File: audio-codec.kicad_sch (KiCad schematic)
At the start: 15 parts, among them J1 AudioJack2_Ground, J2 AudioJack2_Ground, U4 XTAC5112IRGER

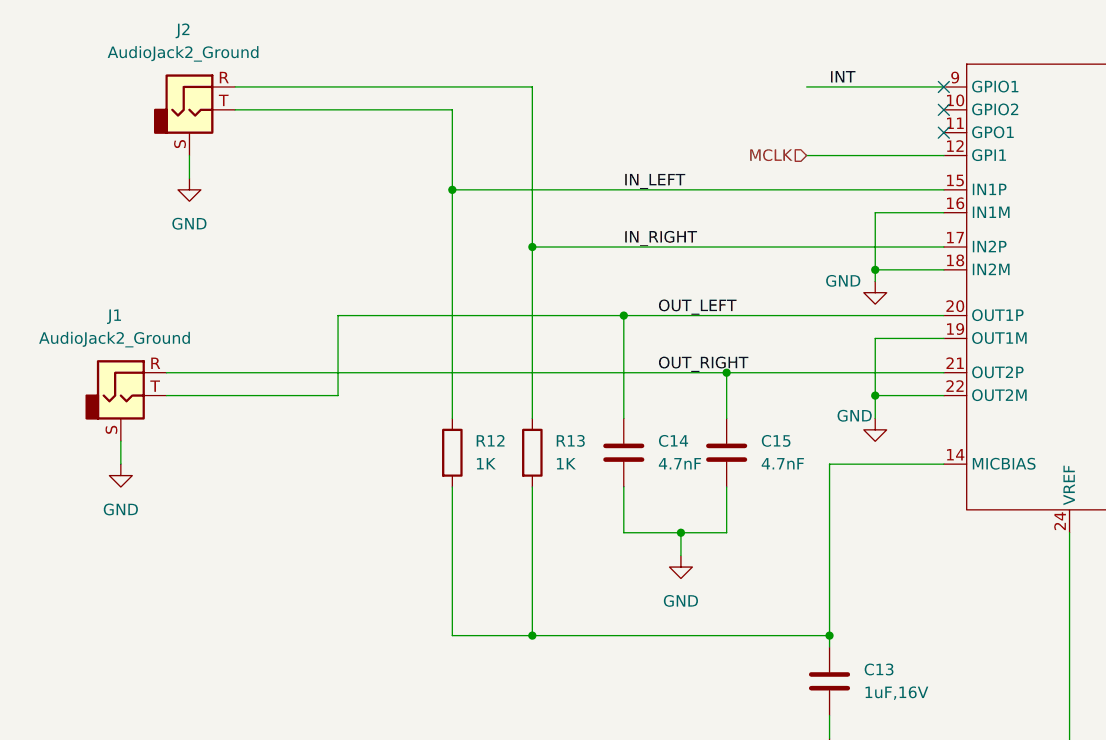
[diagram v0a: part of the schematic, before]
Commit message: Resolved #6: Added connection options for IN_COMMON and OUT_COMMON for audio codec
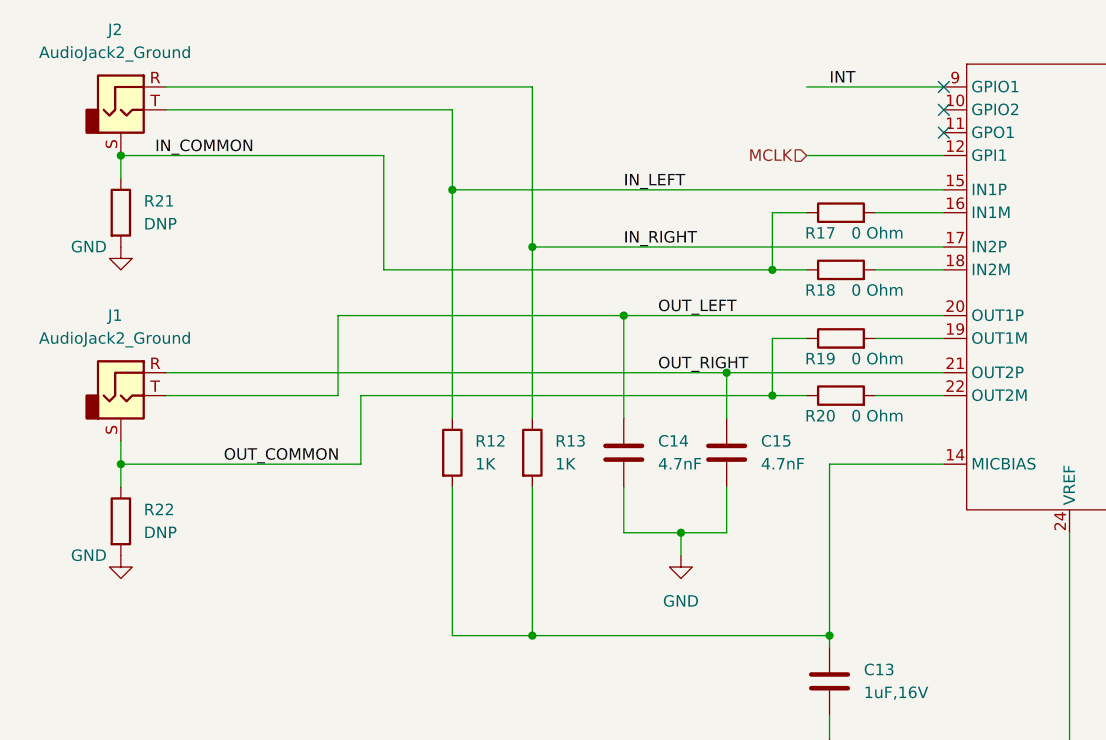
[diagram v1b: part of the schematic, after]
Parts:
- added R17, R18, R19, R20: 0 Ohm, Resistor_SMD:R_0603_1608Metric, symbol Device:R
- added R21, R22: DNP, Resistor_SMD:R_0603_1608Metric, symbol Device:R
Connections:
- net GND: now also R21.2, R22.2; no longer J1.S, J2.S, U4.16 (IN1M), U4.18 (IN2M), U4.19 (OUT1M), U4.22 (OUT2M)
- new net: R20.2, U4.22 (OUT2M)
- new net: R19.2, U4.19 (OUT1M)
- new net: R18.2, U4.18 (IN2M)
- new net: R17.2, U4.16 (IN1M)
- new net IN_COMMON: J2.S, R17.1, R18.1, R21.1
- new net OUT_COMMON: J1.S, R19.1, R20.1, R22.1
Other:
- moved on the sheet: J2

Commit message: Back-annotate BOM from CircuitHub
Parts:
- C13, C16: MPN (none) -> CC0603KRX7R7BB105; Manufacturer (none) -> Yageo
- C14, C15: MPN (none) -> CC0603KRX7R9BB472; Manufacturer (none) -> Yageo
- C17, C19, C21: MPN (none) -> CC0603MRX5R7BB106; Manufacturer (none) -> Yageo
- C18, C20, C22: MPN (none) -> CC0603KRX7R7BB104; Manufacturer (none) -> Yageo
- J1, J2: MPN (none) -> SJ-3523-SMT-TR; Manufacturer (none) -> CUI Devices
- R12, R13: MPN (none) -> CRCW06031K00JNEA; Manufacturer (none) -> Vishay
- R17, R18, R19, R20: MPN (none) -> CRCW06030000Z0EA; Manufacturer (none) -> Vishay
- R21, R22: now not fitted
- U4: MPN (none) -> TAC5112IRGER; Manufacturer (none) -> Texas Instruments

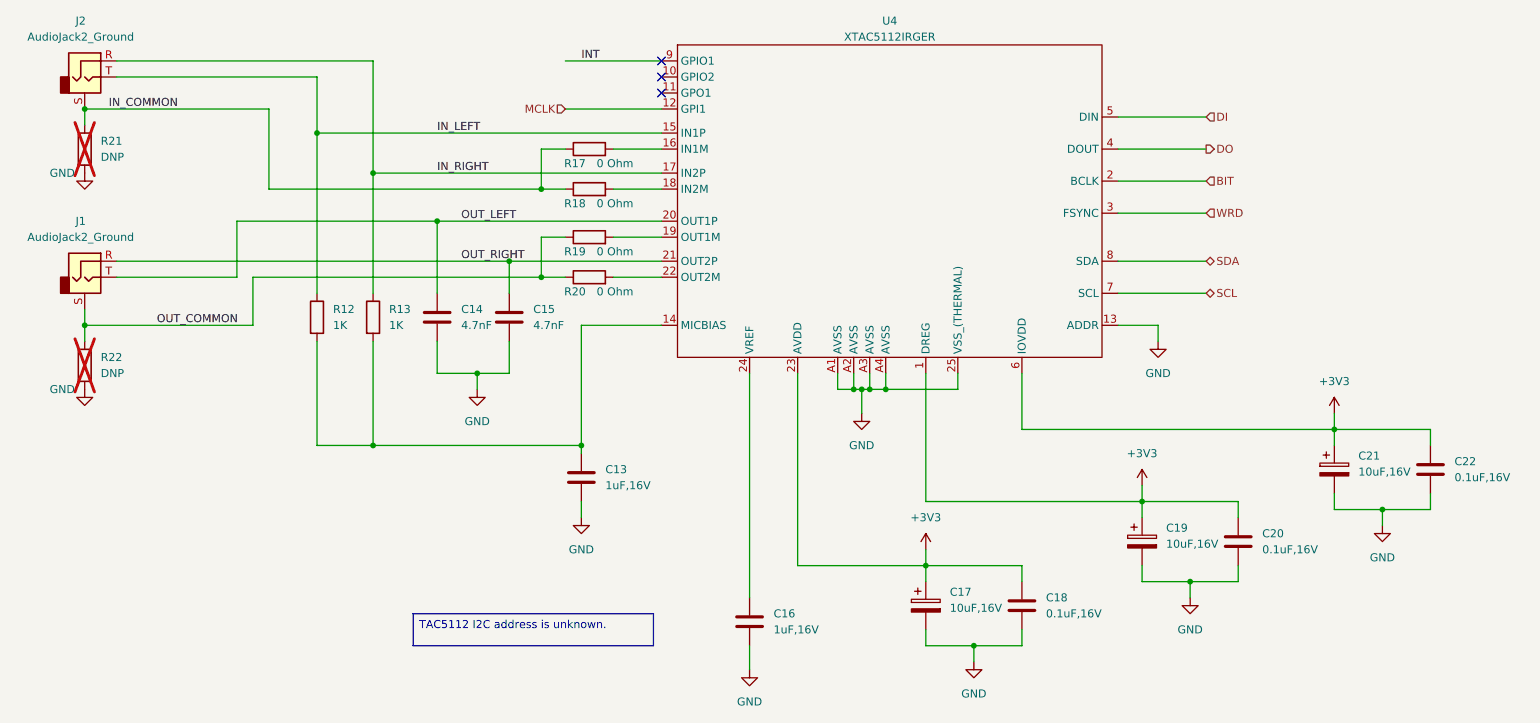
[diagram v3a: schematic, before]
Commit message: added series caps per issue 17
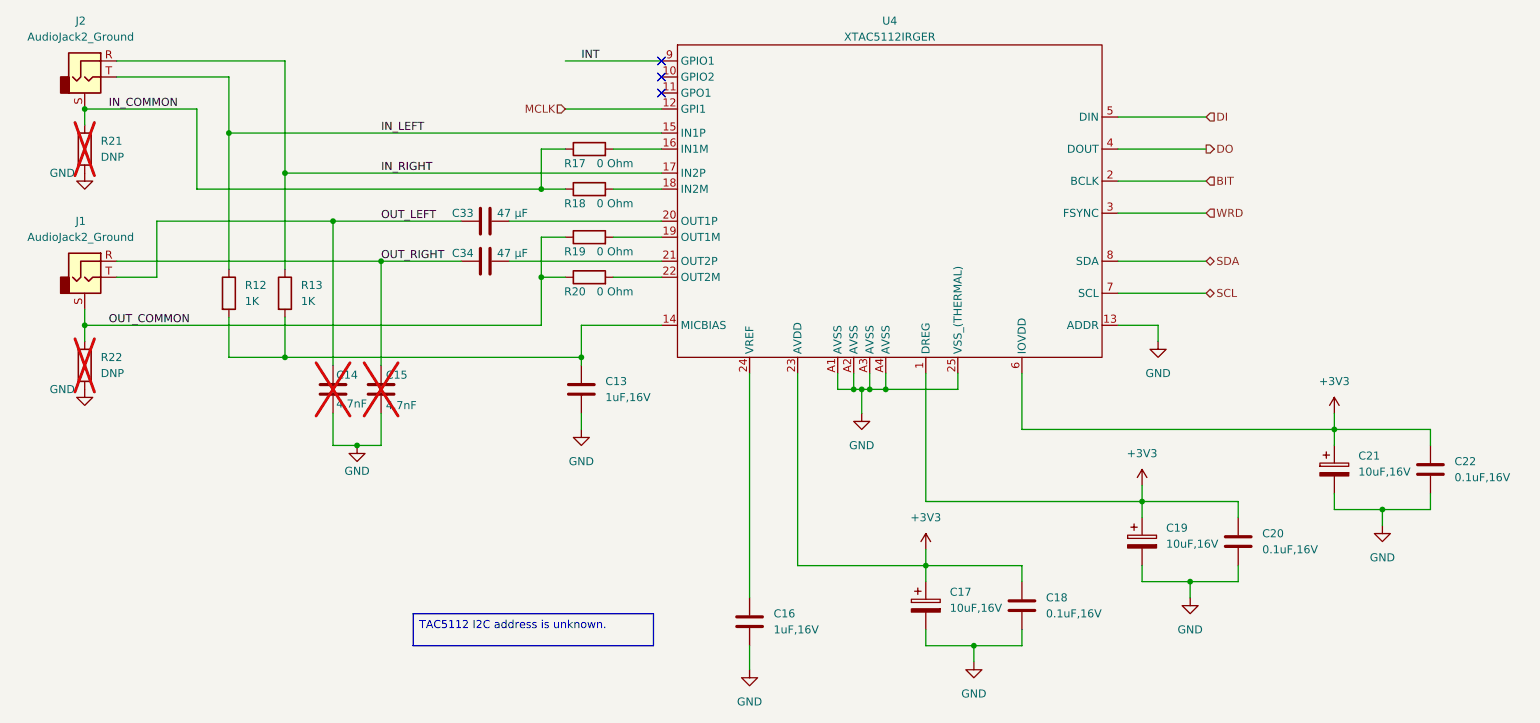
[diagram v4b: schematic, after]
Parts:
- added C33, C34: 47 µF, Capacitor_SMD:C_0603_1608Metric, symbol Device:C
- C14, C15: now not fitted
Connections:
- net OUT_LEFT: now also C33.1; no longer U4.20 (OUT1P)
- net OUT_RIGHT: now also C34.1; no longer U4.21 (OUT2P)
- new net: C33.2, U4.20 (OUT1P)
- new net: C34.2, U4.21 (OUT2P)
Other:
- moved on the sheet: C13, R12, R13

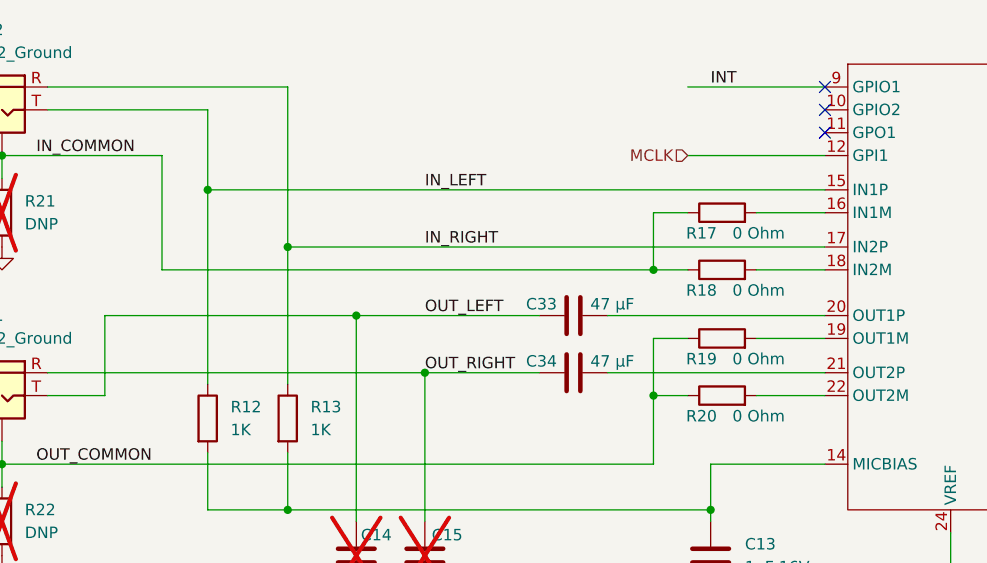
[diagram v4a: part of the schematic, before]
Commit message: Added zero ohm resistors to XTAC5112 inputs
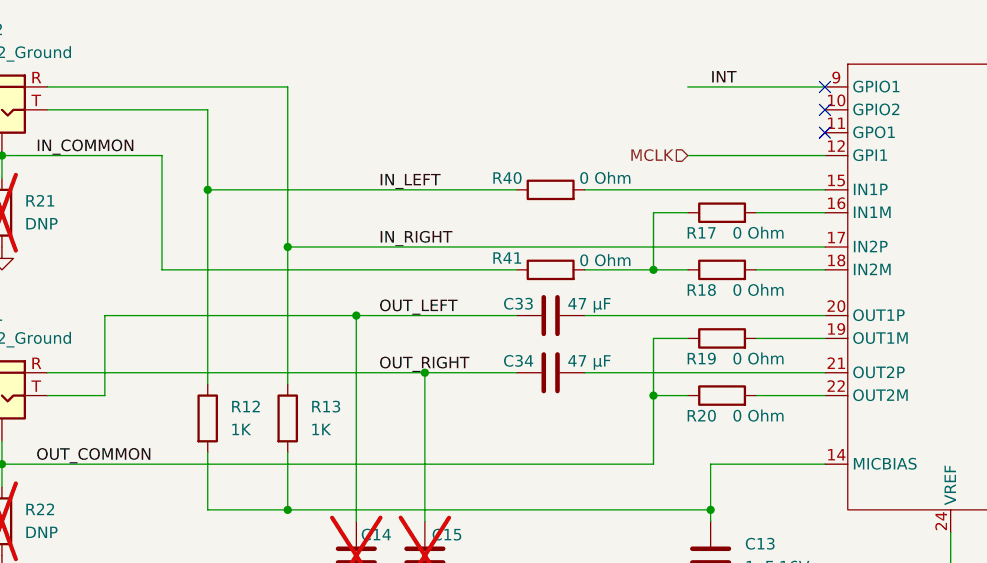
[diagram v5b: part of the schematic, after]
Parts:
- added R40, R41: 0 Ohm, Resistor_SMD:R_0603_1608Metric, symbol Device:R
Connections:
- net IN_COMMON: now also R41.1; no longer R17.1, R18.1
- net IN_LEFT: now also R40.1; no longer U4.15 (IN1P)
- new net: R40.2, U4.15 (IN1P)
- new net: R17.1, R18.1, R41.2
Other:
- moved on the sheet: C33, C34
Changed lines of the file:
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@@
 	(wire
 		(pts
+			(xy 96.52 71.12) (xy 123.19 71.12)
+		)
+		(stroke
+			(width 0)
+			(type default)
+		)
+	)
+	(wire
+		(pts
 			(xy 195.58 78.74) (xy 209.55 78.74)
 		)
@@
 	(wire
 		(pts
-			(xy 71.12 85.09) (xy 91.44 85.09)
+			(xy 96.52 80.01) (xy 104.14 80.01)
+		)
+		(stroke
+			(width 0)
+			(type default)
+		)
+	)
+	(wire
+		(pts
+			(xy 71.12 85.09) (xy 88.9 85.09)
 		)
 		(stroke
@@
 	(wire
 		(pts
-			(xy 99.06 91.44) (xy 123.19 91.44)
+			(xy 96.52 91.44) (xy 123.19 91.44)
 		)
 		(stroke
@@
 	(wire
 		(pts
-			(xy 78.74 91.44) (xy 91.44 91.44)
+			(xy 78.74 91.44) (xy 88.9 91.44)
 		)
 		(stroke
@@
 	(wire
 		(pts
-			(xy 49.53 80.01) (xy 104.14 80.01)
+			(xy 49.53 80.01) (xy 88.9 80.01)
 		)
 		(stroke
@@
 	(wire
 		(pts
-			(xy 54.61 71.12) (xy 123.19 71.12)
+			(xy 54.61 71.12) (xy 88.9 71.12)
 		)
 		(stroke
@@
 	(wire
 		(pts
-			(xy 99.06 85.09) (xy 123.19 85.09)
+			(xy 96.52 85.09) (xy 123.19 85.09)
 		)
 		(stroke
@@
 	)
 	(label "IN_RIGHT"
-		(at 78.74 77.47 0)
+		(at 73.66 77.47 0)
 		(effects
 			(font
@@
 	)
 	(label "OUT_RIGHT"
-		(at 78.74 91.44 0)
+		(at 73.66 91.44 0)
 		(effects
 			(font
@@
 	)
 	(label "OUT_LEFT"
-		(at 78.74 85.09 0)
+		(at 73.66 85.09 0)
 		(effects
 			(font
@@
 	)
 	(label "IN_LEFT"
-		(at 78.74 71.12 0)
+		(at 73.66 71.12 0)
 		(effects
 			(font
@@
 	)
 	(symbol
+		(lib_id "Device:R")
+		(at 92.71 71.12 90)
+		(unit 1)
+		(exclude_from_sim no)
+		(in_bom yes)
+		(on_board yes)
+		(dnp no)
+		(property "Reference" "R40"
+			(at 87.884 69.85 90)
+			(effects
+				(font
+					(size 1.27 1.27)
+				)
+			)
+		)
+		(property "Value" "0 Ohm"
+			(at 98.806 69.85 90)
+			(effects
+				(font
+					(size 1.27 1.27)
+				)
+			)
+		)
+		(property "Footprint" "Resistor_SMD:R_0603_1608Metric"
+			(at 92.71 72.898 90)
+			(effects
+				(font
+					(size 1.27 1.27)
+				)
+				(hide yes)
+			)
+		)
+		(property "Datasheet" "~"
+			(at 92.71 71.12 0)
+			(effects
+				(font
+					(size 1.27 1.27)
+				)
+				(hide yes)
+			)
+		)
+		(property "Description" "Resistor"
+			(at 92.71 71.12 0)
+			(effects
+				(font
+					(size 1.27 1.27)
+				)
+				(hide yes)
+			)
+		)
+		(property "MPN" "CRCW06030000Z0EA"
+			(at 92.71 71.12 0)
+			(effects
+				(font
+					(size 1.27 1.27)
+				)
+				(hide yes)
+			)
+		)
+		(property "Manufacturer" "Vishay"
+			(at 92.71 71.12 0)
+			(effects
+				(font
+					(size 1.27 1.27)
+				)
+				(hide yes)
+			)
+		)
+		(pin "2"
+		)
+		(pin "1"
+		)
+		(instances
+			(project "jkembedded-audio-board"
+				(path "/df100556-b288-4cb1-b69f-c0734132cb90/f904953f-335e-4512-b297-b8d4a411c7e1"
+					(reference "R40")
+					(unit 1)
+				)
+			)
+		)
+	)
+	(symbol
 		(lib_id "Device:C")
 		(at 214.63 135.89 0)
@@
 	(symbol
 		(lib_id "Device:C")
-		(at 95.25 85.09 90)
+		(at 92.71 85.09 90)
 		(unit 1)
 		(exclude_from_sim no)
@@
 		(dnp no)
 		(property "Reference" "C33"
-			(at 91.694 83.82 90)
+			(at 89.154 83.82 90)
 			(effects
 				(font
@@
 		)
 		(property "Value" "47 µF"
-			(at 99.568 83.82 90)
+			(at 97.028 83.82 90)
 			(effects
 				(font
@@
 		)
 		(property "Footprint" "Capacitor_SMD:C_0603_1608Metric"
-			(at 99.06 84.1248 0)
+			(at 96.52 84.1248 0)
 			(effects
 				(font
@@
 		)
 		(property "Datasheet" "~"
-			(at 95.25 85.09 0)
+			(at 92.71 85.09 0)
 			(effects
 				(font
@@
 		)
 		(property "Description" "CAP CER 47UF 10V 20% X5R 0805"
-			(at 95.25 85.09 0)
+			(at 92.71 85.09 0)
 			(effects
 				(font
@@
 		)
 		(property "MPN" "GRM21BR61A476ME15L"
-			(at 95.25 85.09 0)
+			(at 92.71 85.09 0)
 			(effects
 				(font
@@
 		)
 		(property "Manufacturer" "Murata Electronics"
-			(at 95.25 85.09 0)
+			(at 92.71 85.09 0)
 			(effects
 				(font
@@
 	(symbol
 		(lib_id "Device:C")
-		(at 95.25 91.44 90)
+		(at 92.71 91.44 90)
 		(unit 1)
 		(exclude_from_sim no)
@@
 		(dnp no)
 		(property "Reference" "C34"
-			(at 91.694 90.17 90)
+			(at 89.154 90.17 90)
 			(effects
 				(font
@@
 		)
 		(property "Value" "47 µF"
-			(at 99.568 90.17 90)
+			(at 97.028 90.17 90)
 			(effects
 				(font
@@
 		)
 		(property "Footprint" "Capacitor_SMD:C_0603_1608Metric"
-			(at 99.06 90.4748 0)
+			(at 96.52 90.4748 0)
 			(effects
 				(font
@@
 		)
 		(property "Datasheet" "~"
-			(at 95.25 91.44 0)
+			(at 92.71 91.44 0)
 			(effects
 				(font
@@
 		)
 		(property "Description" "CAP CER 47UF 10V 20% X5R 0805"
-			(at 95.25 91.44 0)
+			(at 92.71 91.44 0)
 			(effects
 				(font
@@
 		)
 		(property "MPN" "GRM21BR61A476ME15L"
-			(at 95.25 91.44 0)
+			(at 92.71 91.44 0)
 			(effects
 				(font
@@
 		)
 		(property "Manufacturer" "Murata Electronics"
-			(at 95.25 91.44 0)
+			(at 92.71 91.44 0)
 			(effects
 				(font
@@
 					(unit 1)
 				)
+			)
+		)
+	)
+	(symbol
+		(lib_id "Device:R")
+		(at 92.71 80.01 90)
+		(unit 1)
+		(exclude_from_sim no)
+		(in_bom yes)
+		(on_board yes)
+		(dnp no)
+		(property "Reference" "R41"
+			(at 87.884 78.74 90)
+			(effects
+				(font
+					(size 1.27 1.27)
+				)
+			)
+		)
+		(property "Value" "0 Ohm"
+			(at 98.806 78.994 90)
+			(effects
+				(font
+					(size 1.27 1.27)
+				)
+			)
+		)
+		(property "Footprint" "Resistor_SMD:R_0603_1608Metric"
+			(at 92.71 81.788 90)
+			(effects
+				(font
+					(size 1.27 1.27)
+				)
+				(hide yes)
+			)
+		)
+		(property "Datasheet" "~"
+			(at 92.71 80.01 0)
+			(effects
+				(font
+					(size 1.27 1.27)
+				)
+				(hide yes)
+			)
+		)
+		(property "Description" "Resistor"
+			(at 92.71 80.01 0)
+			(effects
+				(font
+					(size 1.27 1.27)
+				)
+				(hide yes)
+			)
+		)
+		(property "MPN" "CRCW06030000Z0EA"
+			(at 92.71 80.01 0)
+			(effects
+				(font
+					(size 1.27 1.27)
+				)
+				(hide yes)
+			)
+		)
+		(property "Manufacturer" "Vishay"
+			(at 92.71 80.01 0)
+			(effects
+				(font
+					(size 1.27 1.27)
+				)
+				(hide yes)
+			)
+		)
+		(pin "2"
+		)
+		(pin "1"
+		)
+		(instances
+			(project "jkembedded-audio-board"
+				(path "/df100556-b288-4cb1-b69f-c0734132cb90/f904953f-335e-4512-b297-b8d4a411c7e1"
+					(reference "R41")
+					(unit 1)
+				)

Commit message: In process routing edits
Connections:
- net IN_COMMON: now also R17.1, R18.1; no longer R41.1
- net IN_RIGHT: now also R41.1; no longer U4.17 (IN2P)
- new net: R41.2, U4.17 (IN2P)
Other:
- moved on the sheet: R41
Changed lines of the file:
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@@
 	(wire
 		(pts
-			(xy 96.52 80.01) (xy 104.14 80.01)
-		)
-		(stroke
-			(width 0)
-			(type default)
-		)
-	)
-	(wire
-		(pts
 			(xy 71.12 85.09) (xy 88.9 85.09)
 		)
@@
 	(wire
 		(pts
-			(xy 63.5 77.47) (xy 123.19 77.47)
+			(xy 63.5 77.47) (xy 88.9 77.47)
 		)
 		(stroke
@@
 	(wire
 		(pts
+			(xy 96.52 77.47) (xy 123.19 77.47)
+		)
+		(stroke
+			(width 0)
+			(type default)
+		)
+	)
+	(wire
+		(pts
 			(xy 195.58 91.44) (xy 209.55 91.44)
 		)
@@
 	(wire
 		(pts
-			(xy 49.53 80.01) (xy 88.9 80.01)
+			(xy 49.53 80.01) (xy 104.14 80.01)
 		)
 		(stroke
@@
 	(symbol
 		(lib_id "Device:R")
-		(at 92.71 80.01 90)
+		(at 92.71 77.47 90)
 		(unit 1)
 		(exclude_from_sim no)
@@
 		(dnp no)
 		(property "Reference" "R41"
-			(at 87.884 78.74 90)
+			(at 87.884 76.2 90)
 			(effects
 				(font
@@
 		)
 		(property "Value" "0 Ohm"
-			(at 98.806 78.994 90)
+			(at 98.806 76.454 90)
 			(effects
 				(font
@@
 		)
 		(property "Footprint" "Resistor_SMD:R_0603_1608Metric"
-			(at 92.71 81.788 90)
+			(at 92.71 79.248 90)
 			(effects
 				(font
@@
 		)
 		(property "Datasheet" "~"
-			(at 92.71 80.01 0)
+			(at 92.71 77.47 0)
 			(effects
 				(font
@@
 		)
 		(property "Description" "Resistor"
-			(at 92.71 80.01 0)
+			(at 92.71 77.47 0)
 			(effects
 				(font
@@
 		)
 		(property "MPN" "CRCW06030000Z0EA"
-			(at 92.71 80.01 0)
+			(at 92.71 77.47 0)
 			(effects
 				(font
@@
 		)
 		(property "Manufacturer" "Vishay"
-			(at 92.71 80.01 0)
+			(at 92.71 77.47 0)
 			(effects
 				(font
